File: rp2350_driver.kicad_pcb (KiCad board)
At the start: 6 copper layers, 76 x 46.4 mm, 241 parts, among them J1 Power Input, J2 CAN2 PLUG, J201 Estop Conn, J202 USB_C_Receptacle_USB2.0, J203 Conn_01x06, J204 SM03B-SRSS-TB, J205 Power Output, J206 SM03B-SRSS-TB, J207 Conn_01x03, J208 Conn_01x03, J21 Power Input, J3 Power Input, Q1 Q_PNP_BEC, Q2 Q_PNP_BEC, Q201 Q_PNP_BEC, Q3 Q_PNP_BEC, SW201 Boot, SW202 Reset, U1 INA240A1D, U12 MAX3485, U2 EG3113, U201 EG3113, U202 SPX3819M5-L-3-3, U203 RP2350_80QFN, U204 W25Q16JV, U205 USBLC6-4SC6, U21 INA240A1D, U3 USBLC6-2P6, U4 TX4137, U44 INA240A1D, U5 EG3113, U6 CA-IS3052G, U8 EG3113, Y201 ABM8-272-T3

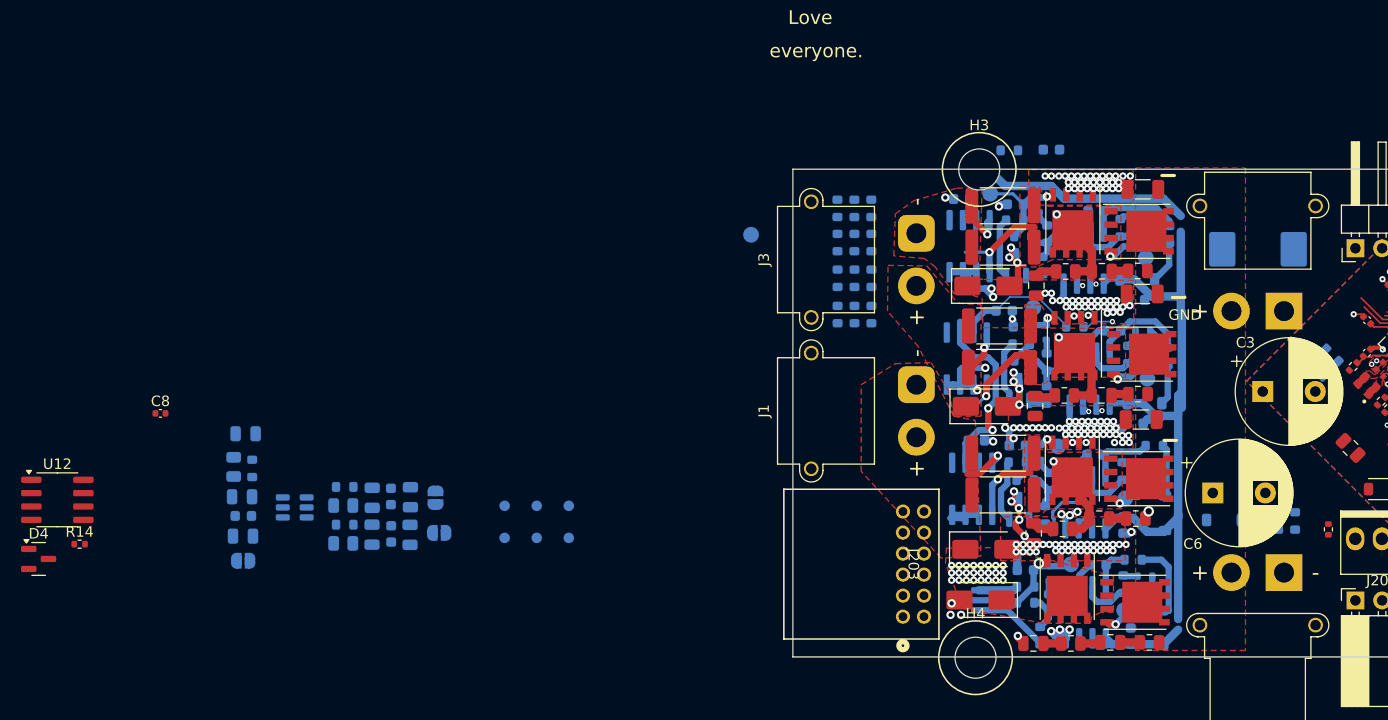
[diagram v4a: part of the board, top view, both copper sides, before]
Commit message: progress on encoder connector and differential IC selection
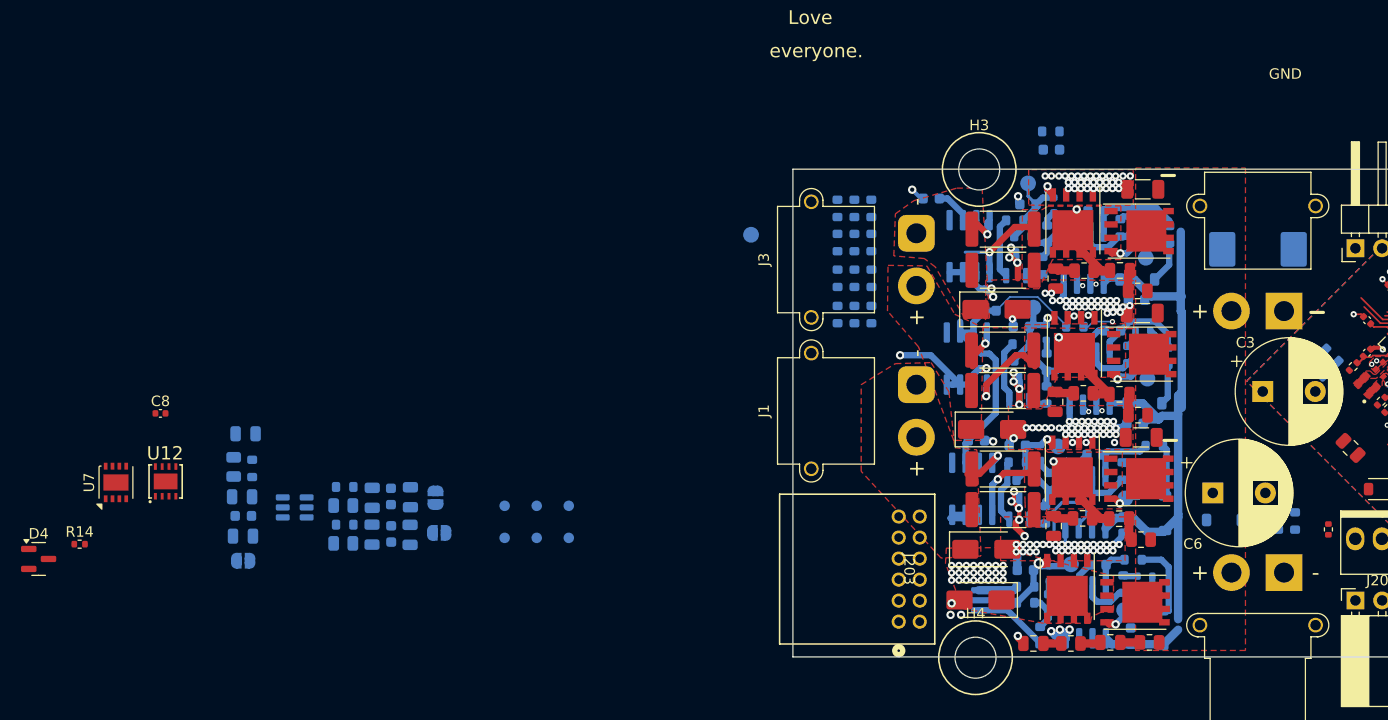
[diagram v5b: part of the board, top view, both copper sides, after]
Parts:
- added U7: MCP2542WFDxMF, Package_DFN_QFN:DFN-8-1EP_3x3mm_P0.65mm_EP1.55x2.4mm, F.Cu at (48.1, 111.8)
- U12: value MAX3485 -> ~; footprint Package_SO:SOIC-8_3.9x4.9mm_P1.27mm -> parts:DFN-8_L3.0-W3.0-P0.65-BL-EP
- moved U12 10.4 mm to (52.8, 111.7)
- moved R45 4.34 mm to (137.0, 78.4)
- moved TP66 3.73 mm to (134.9, 83.3)
- moved C74 2.90 mm to (125.7, 84.8)
- moved D9 2.36 mm to (131.9, 95.3)
- moved R5 2.32 mm to (132.5, 99.2)
- moved D8 2.26 mm to (131.5, 106.8)
- moved R114 2.22 mm to (132.5, 87.7)
- moved R4 2.22 mm to (132.5, 103.1)
- moved R109 2.20 mm to (132.5, 91.6)
- moved R87 2.15 mm to (140.1, 115.2)
- moved R86 2.06 mm to (145.6, 117.2)
- moved C102 2.02 mm to (137.3, 115.9)
- moved R91 2.00 mm to (145.3, 105.4)
- moved C104 1.97 mm to (137.5, 92.4)
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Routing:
- net +5V: track 91.6 -> 72.5 mm
- net GND: track 92.0 -> 95.2 mm, vias 186 -> 174
- net /B_P: track 24.6 -> 23.1 mm
- net /A_P: track 16.1 -> 17.0 mm
- net /C_N: track 4.89 -> 3.95 mm
- net +3V3: track 78.4 -> 77.7 mm, vias 2 -> 0
- net /2CGH: track 6.43 -> 5.92 mm
- net VMOT: vias 1 -> 0

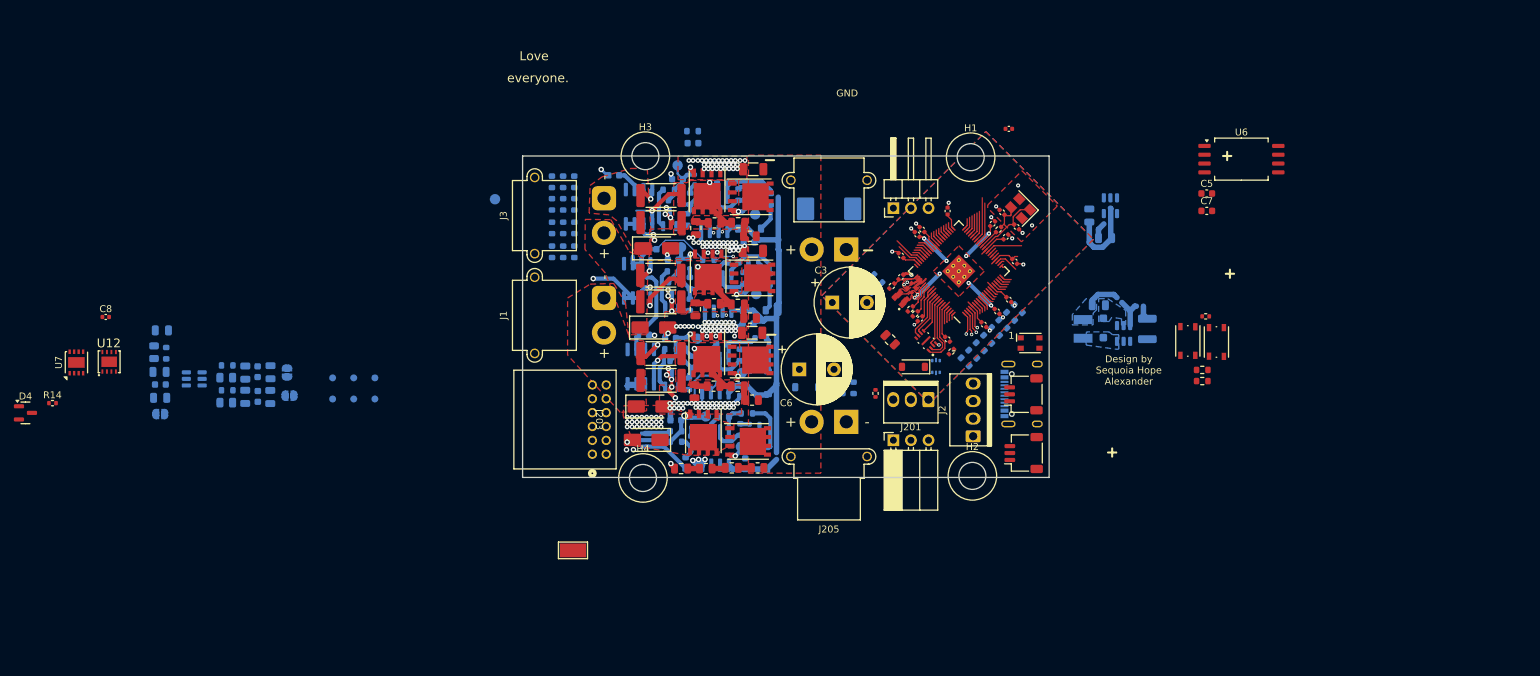
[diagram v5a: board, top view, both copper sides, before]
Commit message: update encoder section - multi encoder port maybe sorted
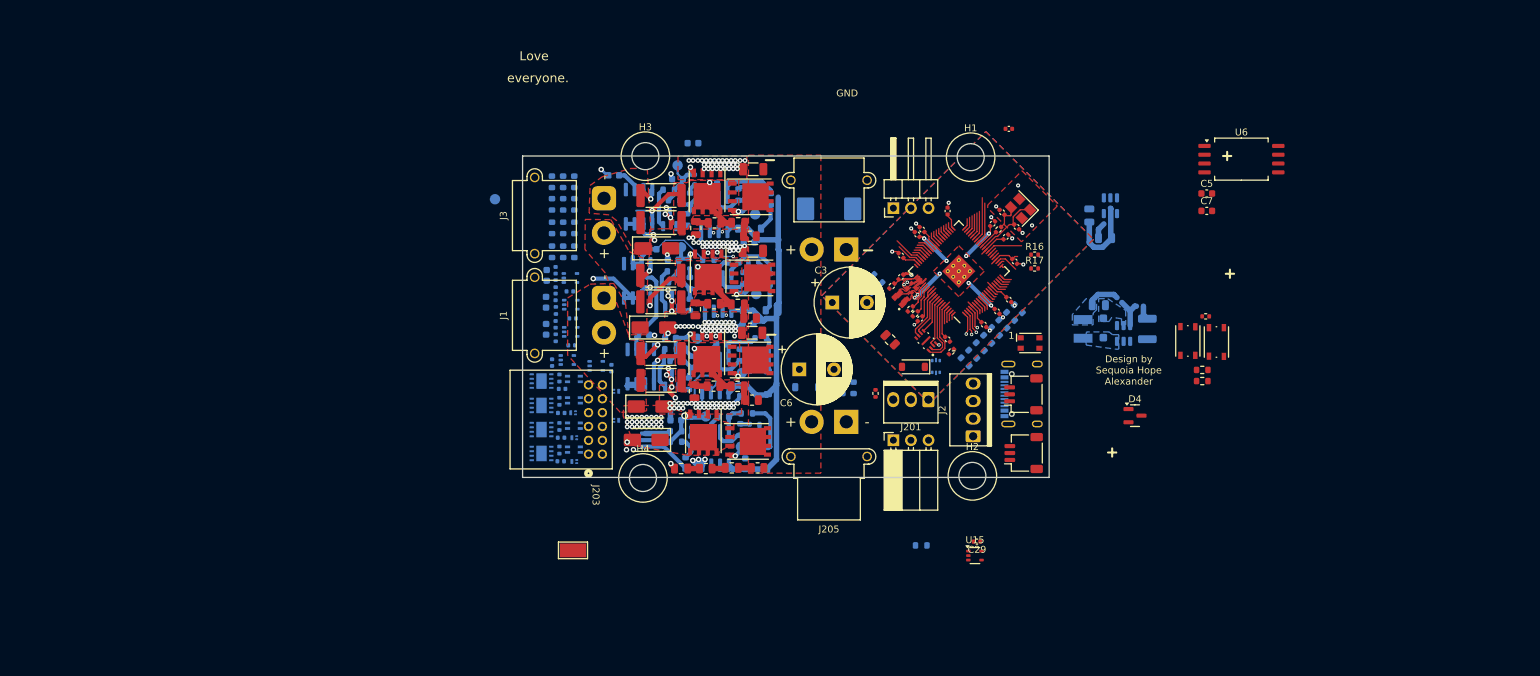
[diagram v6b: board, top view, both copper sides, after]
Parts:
- removed C223: 10u, Capacitor_SMD:C_0805_2012Metric
- removed C224, C227, C230: 22nF, Capacitor_SMD:C_0805_2012Metric
- removed C225, C228, C231: 47p, Capacitor_SMD:C_0603_1608Metric
- removed C226, C229, C232: ~, Capacitor_SMD:C_0805_2012Metric
- removed JP201, JP202, JP203: SolderJumper_2_Open, Jumper:SolderJumper-2_P1.3mm_Open_RoundedPad1.0x1.5mm
- removed R214, R216, R218: 10k, Resistor_SMD:R_0603_1608Metric
- removed R215, R217, R219: ~, Resistor_SMD:R_0805_2012Metric
- removed TP201, TP202, TP203, TP204, TP205, TP206: TestPoint, TestPoint:TestPoint_Pad_D1.0mm
- removed U205: USBLC6-4SC6, Package_TO_SOT_SMD:SOT-23-6
- added C14: 100n, Capacitor_SMD:C_0402_1005Metric, B.Cu at (119.7, 105.4)
- added C16: 47p, Capacitor_SMD:C_0402_1005Metric, B.Cu at (117.3, 102.3)
- added C18: 100n, Capacitor_SMD:C_0402_1005Metric, B.Cu at (118.0, 126.1)
- added C19: 47p, Capacitor_SMD:C_0402_1005Metric, B.Cu at (117.3, 106.3)
- added C20: DNP, Capacitor_SMD:C_0603_1608Metric, B.Cu at (115.9, 107.0)
- added C21: 100n, Capacitor_SMD:C_0402_1005Metric, B.Cu at (118.1, 119.1)
- added C22: 100n, Capacitor_SMD:C_0402_1005Metric, B.Cu at (125.3, 112.6)
- added C23: 100n, Capacitor_SMD:C_0402_1005Metric, B.Cu at (116.8, 111.8)
- added C24: 100n, Capacitor_SMD:C_0402_1005Metric, B.Cu at (118.2, 115.6)
- added C26: 100n, Capacitor_SMD:C_0402_1005Metric, B.Cu at (119.6, 109.3)
- added C27: DNP, Capacitor_SMD:C_0603_1608Metric, B.Cu at (115.9, 103.1)
- added C28: 100n, Capacitor_SMD:C_0402_1005Metric, B.Cu at (119.3, 101.5)
- added C29: 100n, Capacitor_SMD:C_0402_1005Metric, F.Cu at (178.1, 137.7)
- added C31: 47p, Capacitor_SMD:C_0402_1005Metric, B.Cu at (117.3, 98.5)
- added C32: DNP, Capacitor_SMD:C_0603_1608Metric, B.Cu at (116.0, 99.2)
- added D19: 5V TVS, Package_TO_SOT_SMD:SOT-883, B.Cu at (119.8, 119.1)
- added D20: 5V TVS, Package_TO_SOT_SMD:SOT-883, B.Cu at (120.0, 122.7)
- added D21: 5V TVS, Package_TO_SOT_SMD:SOT-883, B.Cu at (120.0, 126.1)
- added D22: 5V TVS, Package_TO_SOT_SMD:SOT-883, B.Cu at (126.0, 120.2)
- added D23: 5V TVS, Package_TO_SOT_SMD:SOT-883, B.Cu at (126.0, 116.0)
- added FL1: DLW21SN900SQ2L, parts:FILTER-SMD_4P-L2.0-W1.2-BL_DLW21H, B.Cu at (119.9, 117.3)
- added FL2: DLW21SN900SQ2L, parts:FILTER-SMD_4P-L2.0-W1.2-BL_DLW21H, B.Cu at (119.9, 120.9)
- added FL3: DLW21SN900SQ2L, parts:FILTER-SMD_4P-L2.0-W1.2-BL_DLW21H, B.Cu at (119.9, 124.4)
- added FL4: DLW21SN900SQ2L, parts:FILTER-SMD_4P-L2.0-W1.2-BL_DLW21H, B.Cu at (119.9, 114.2)
- added R15: 100R 0402, Resistor_SMD:R_0402_1005Metric, B.Cu at (117.8, 121.0)
- added R16: 10k, Resistor_SMD:R_0402_1005Metric, F.Cu at (186.4, 96.2)
- added R17: 10k, Resistor_SMD:R_0402_1005Metric, F.Cu at (186.4, 98.2)
- added R19: 10k, Resistor_SMD:R_0402_1005Metric, B.Cu at (117.3, 104.3)
- added R20: 10k, Resistor_SMD:R_0402_1005Metric, B.Cu at (117.3, 108.2)
- added R35: 100R 0402, Resistor_SMD:R_0402_1005Metric, B.Cu at (117.8, 124.4)
- added R40: 100R 0402, Resistor_SMD:R_0402_1005Metric, B.Cu at (117.8, 114.0)
- added R41: 10k, Resistor_SMD:R_0402_1005Metric, B.Cu at (117.3, 100.4)
- added U10: SIT3088ETK, parts:DFN-8_L3.0-W3.0-P0.65-BL-EP, B.Cu at (115.2, 114.5)
- added U11: TS5A3159DCK, Package_TO_SOT_SMD:SOT-353_SC-70-5, B.Cu at (119.0, 111.5)
- added U13: TS5A3159DCK, Package_TO_SOT_SMD:SOT-353_SC-70-5, B.Cu at (119.5, 107.4)
- added U14: TS5A3159DCK, Package_TO_SOT_SMD:SOT-353_SC-70-5, B.Cu at (119.5, 103.5)
- added U15: TS5A3159DCK, Package_TO_SOT_SMD:SOT-353_SC-70-5, F.Cu at (177.8, 139.7)
- added U16: TS5A3159DCK, Package_TO_SOT_SMD:SOT-353_SC-70-5, B.Cu at (119.4, 99.6)
- added U17: TS5A3159DCK, Package_TO_SOT_SMD:SOT-353_SC-70-5, B.Cu at (123.1, 112.3)
- added U9: SIT3088ETK, parts:DFN-8_L3.0-W3.0-P0.65-BL-EP, B.Cu at (115.2, 124.9)
- C8, R14: moved to B.Cu
- U12: value ~ -> SIT3088ETK; moved to B.Cu
- U7: value MCP2542WFDxMF -> SIT3088ETK; footprint Package_DFN_QFN:DFN-8-1EP_3x3mm_P0.65mm_EP1.55x2.4mm -> parts:DFN-8_L3.0-W3.0-P0.65-BL-EP; moved to B.Cu
- moved D4 160.2 mm to (200.9, 119.5)
- moved R14 73.2 mm to (117.8, 117.4), turned to 90 degrees
- moved R45 68.3 mm to (170.0, 138.2)
- moved C8 68.0 mm to (118.1, 122.7)
- moved U7 67.8 mm to (115.2, 121.5)
- moved U12 62.7 mm to (115.2, 118.0), turned to 90 degrees
- moved J203 0.55 mm to (122.0, 125.0)
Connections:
- net /GPIO30 renamed /TH_SW_1
- C5 pad 2: +5V_ISO_FILT -> +5V_ISO
- C7 pad 2: +5V_ISO_FILT -> +5V_ISO
- J203 pad 1: unconnected-(J203-Pin_1-Pad1) -> /ENC_C_N
- J203 pad 10: unconnected-(J203-Pin_10-Pad10) -> /I2C_SCL
- J203 pad 11: (no net) -> /ENC_A_P
- J203 pad 12: (no net) -> /MOT_TH
- J203 pad 2: unconnected-(J203-Pin_2-Pad2) -> GND
- J203 pad 3: unconnected-(J203-Pin_3-Pad3) -> /ENC_C_P
- J203 pad 4: unconnected-(J203-Pin_4-Pad4) -> /V_ENC
- J203 pad 5: unconnected-(J203-Pin_5-Pad5) -> /ENC_B_N
- J203 pad 6: unconnected-(J203-Pin_6-Pad6) -> /ENC_D_P
- J203 pad 7: unconnected-(J203-Pin_7-Pad7) -> /ENC_B_P
- J203 pad 8: unconnected-(J203-Pin_8-Pad8) -> /ENC_D_N
- J203 pad 9: unconnected-(J203-Pin_9-Pad9) -> /ENC_A_N
- R14 pad 1: /ENC_A_N -> Net-(U12-B)
- R14 pad 2: /ENC_A_P -> Net-(U12-A)
- TH1 pad 2: /TH1_SENSE -> Net-(U15-NC)
- U12 pad 1: unconnected-(U12-RO-Pad1) -> /ENC1_D
- U12 pad 2: unconnected-(U12-~{RE}-Pad2) -> /ENC1_E
- U12 pad 3: unconnected-(U12-DE-Pad3) -> /ENC1_E
- U12 pad 4: unconnected-(U12-DI-Pad4) -> /ENC1_D
- U12 pad 5: unconnected-(U12-GND-Pad5) -> GND
- U12 pad 6: /ENC_A_P -> Net-(U12-A)
- U12 pad 7: /ENC_A_N -> Net-(U12-B)
- U12 pad 8: unconnected-(U12-VCC-Pad8) -> +3V3
- U203 pad 16: /GPIO16 -> /ENC1_D
- U203 pad 17: /GPIO17 -> /ENC2_D
- U203 pad 18: /GPIO18 -> /ENC3_D
- U203 pad 19: /GPIO19 -> /ENC4_D
- U203 pad 22: /GPIO22 -> /I2C_SDA
- U203 pad 23: /GPIO23 -> /I2C_SCL
- U203 pad 27: /GPIO26 -> /ENC1_E
- U203 pad 28: /GPIO27 -> /ENC2_E
- U203 pad 36: /GPIO28 -> /ENC3_E
- U203 pad 37: /GPIO29 -> /ENC4_E
- U203 pad 39: /GPIO31 -> unconnected-(U203-GPIO31-Pad39)
- U6 pad 8: +5V_ISO_FILT -> +5V_ISO
- U7 pad 1: unconnected-(U7-TXD-Pad1) -> /ENC2_D
- U7 pad 2: Net-(U7-VSS-Pad2) -> /ENC2_E
- U7 pad 3: unconnected-(U7-VDD-Pad3) -> /ENC2_E
- U7 pad 4: unconnected-(U7-RXD-Pad4) -> /ENC2_D
- U7 pad 5: unconnected-(U7-VIO-Pad5) -> GND
- U7 pad 6: unconnected-(U7-CANL-Pad6) -> Net-(U7-A)
- U7 pad 7: unconnected-(U7-CANH-Pad7) -> Net-(U7-B)
- U7 pad 8: unconnected-(U7-STBY-Pad8) -> +3V3
- U7 pad 9: Net-(U7-VSS-Pad2) -> (no net)
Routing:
- net /GPIO27: track 5.26 -> 0.00 mm
- net /ENC2_E: track 0.00 -> 5.26 mm
- net /GPIO28: track 3.69 -> 0.00 mm
- net /ENC3_E: track 0.00 -> 3.69 mm
- net /I2C_SCL: track 0.00 -> 3.41 mm
- net /GPIO23: track 3.41 -> 0.00 mm
- net /GPIO29: track 3.17 -> 0.00 mm
- net /ENC4_E: track 0.00 -> 3.17 mm
- net Net-(U15-NC): track 0.00 -> 2.95 mm, vias 0 -> 1
- net /TH1_SENSE: track 6.90 -> 3.94 mm, vias 1 -> 0
- net unconnected-(U203-GPIO31-Pad39): track 0.00 -> 2.12 mm
- net /GPIO31: track 2.12 -> 0.00 mm
- net /GPIO16: track 1.99 -> 0.00 mm
- net /ENC1_D: track 0.00 -> 1.99 mm
- net /GPIO17: track 1.89 -> 0.00 mm
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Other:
- board text removed: "B"

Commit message: All components in board footprint. Big readme update.
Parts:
- added C30: 100n, Capacitor_SMD:C_0402_1005Metric, B.Cu at (124.7, 113.4)
- added C33: 100n, Capacitor_SMD:C_0402_1005Metric, B.Cu at (121.8, 113.3)
- added C34: 100n, Capacitor_SMD:C_0402_1005Metric, B.Cu at (168.6, 83.8)
- added C35: 100n, Capacitor_SMD:C_0402_1005Metric, B.Cu at (165.8, 83.7)
- added C36: 100n, Capacitor_SMD:C_0402_1005Metric, B.Cu at (182.8, 87.7)
- added R21: 10k, Resistor_SMD:R_0402_1005Metric, B.Cu at (118.6, 105.9)
- added R34: 10k, Resistor_SMD:R_0402_1005Metric, B.Cu at (119.0, 107.9)
- added R37: 10k, Resistor_SMD:R_0402_1005Metric, B.Cu at (122.8, 127.7)
- added R38: 10k, Resistor_SMD:R_0402_1005Metric, B.Cu at (122.8, 126.6)
- added R39: 10k, Resistor_SMD:R_0402_1005Metric, B.Cu at (119.0, 111.9)
- added R42: 10k, Resistor_SMD:R_0402_1005Metric, B.Cu at (118.9, 109.9)
- added R43: 10k, Resistor_SMD:R_0402_1005Metric, B.Cu at (114.0, 103.2)
- added R44: 10k, Resistor_SMD:R_0402_1005Metric, B.Cu at (113.5, 101.7)
- added U18: TS5A3159DCK, Package_TO_SOT_SMD:SOT-353_SC-70-5, B.Cu at (125.2, 111.2)
- added U19: TS5A3159DCK, Package_TO_SOT_SMD:SOT-353_SC-70-5, B.Cu at (122.3, 111.2)
- added U20: TS5A3159DCK, Package_TO_SOT_SMD:SOT-353_SC-70-5, B.Cu at (168.7, 85.9)
- added U22: TS5A3159DCK, Package_TO_SOT_SMD:SOT-353_SC-70-5, B.Cu at (165.7, 85.9)
- C29, C5, C7, D4, R208, R224, R225, U15, U6: moved to B.Cu
- SW201, SW202: footprint Button_Switch_SMD:SW_Push_1P1T_NO_Vertical_Wuerth_434133025816 -> parts:KEY-SMD_4P-L4.2-W3.2-P2.20-LS4.6
- moved TP71 50.5 mm to (162.8, 112.6)
- moved C12 46.8 mm to (155.9, 107.2), turned to -90 degrees
- moved R45 44.8 mm to (164.1, 93.8)
- moved R11 44.3 mm to (157.8, 110.4), turned to 0 degrees
- moved C23 40.7 mm to (154.8, 126.2), turned to 180 degrees
- moved U4 39.6 mm to (159.7, 107.7), turned to 90 degrees
- moved R12 39.6 mm to (160.0, 111.2), turned to 135 degrees
- moved U11 37.8 mm to (154.5, 124.2), turned to 90 degrees
- moved R224 37.2 mm to (173.5, 115.9), turned to -90 degrees
- moved R225 35.5 mm to (175.1, 115.9), turned to -90 degrees
- moved C218 34.1 mm to (169.0, 109.2), turned to -45 degrees
- moved U6 34.0 mm to (184.8, 95.3), turned to -90 degrees
- moved D3 33.8 mm to (162.6, 107.7), turned to -90 degrees
- moved C10 33.3 mm to (163.2, 111.0), turned to 180 degrees
- moved C5 29.0 mm to (186.6, 102.8), turned to 180 degrees
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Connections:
- net /GPIO14 renamed /V_SW
- net /GPIO15 renamed /I2C_SW
- net /GPIO34 renamed /H1_SW
- net /GPIO35 renamed /H2_SW
- net /GPIO36 renamed /H3_SW
- net /GPIO37 renamed /EXT_ANALOG_SW
- FL1 pad 2: /ENC_A_N -> /ENC_A_N_SW
- FL1 pad 3: /ENC_A_P -> /ENC_A_P_SW
- FL2 pad 2: /ENC_B_N -> /ENC_B_N_SW
- FL2 pad 3: /ENC_B_P -> /ENC_B_P_SW
- FL3 pad 2: /ENC_C_N -> /ENC_C_N_SW
- FL3 pad 3: /ENC_C_P -> /ENC_C_P_SW
- FL4 pad 3: /ENC_D_P_SWITCHED -> /ENC_D_P
- U13 pad 3: unconnected-(U13-NC-Pad3) -> /ENC_A_P_SW
- U14 pad 3: unconnected-(U14-NC-Pad3) -> /ENC_A_N_SW
- U14 pad 4: /ENC_B_P -> /ENC_A_N
- U16 pad 3: unconnected-(U16-NC-Pad3) -> /ENC_B_P_SW
- U16 pad 4: /ENC_C_P -> /ENC_B_P
- U17 pad 3: /ENC_D_P_SWITCHED -> /ENC_B_N_SW
- U17 pad 4: /ENC_D_P -> /ENC_B_N
- U203 pad 39: unconnected-(U203-GPIO31-Pad39) -> /HALL1
- U203 pad 40: /GPIO32 -> /HALL2
- U203 pad 42: /GPIO33 -> /HALL3
- U203 pad 47: /GPIO38 -> unconnected-(U203-GPIO38-Pad47)
- U203 pad 48: /GPIO39 -> unconnected-(U203-GPIO39-Pad48)
- U203 pad 55: B_PHASE_SENSE -> /ADC4
- U203 pad 56: C_PHASE_SENSE -> /ADC5
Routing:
- net unconnected-(U203-GPIO31-Pad39): track 2.12 -> 0.00 mm
- net /HALL1: track 0.00 -> 2.12 mm
- net B_PHASE_SENSE: track 2.05 -> 0.00 mm
- net /ADC4: track 0.00 -> 2.05 mm
- net Net-(U4-FB): track 4.99 -> 2.98 mm
- net C_PHASE_SENSE: track 1.95 -> 0.00 mm
- net /ADC5: track 0.00 -> 1.95 mm
- net unconnected-(U203-GPIO39-Pad48): track 0.00 -> 1.91 mm
- net /GPIO39: track 1.91 -> 0.00 mm
- net unconnected-(U203-GPIO38-Pad47): track 0.00 -> 1.81 mm
- net /GPIO38: track 1.81 -> 0.00 mm
- net /HALL2: track 0.00 -> 1.59 mm
- net /GPIO32: track 1.59 -> 0.00 mm
- net /HALL3: track 0.00 -> 1.31 mm
- net /GPIO33: track 1.31 -> 0.00 mm
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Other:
- board text added: "github.com/ sequoia-hope/rp2350-motor-controller"
- board text removed: "github.com/ Twisted-Fields/rp2040-motor-controller"
